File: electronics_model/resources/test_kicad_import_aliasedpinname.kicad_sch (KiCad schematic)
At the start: 3 parts

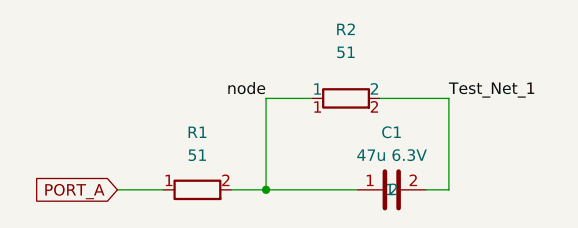
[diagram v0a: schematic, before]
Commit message: unify naming
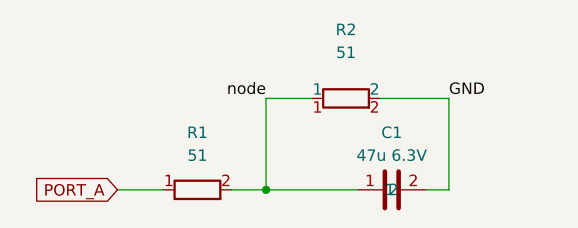
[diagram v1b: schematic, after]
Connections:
- net Test_Net_1 renamed GND
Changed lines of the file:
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@@
     (effects (font (size 1.27 1.27)) (justify right bottom))
   )
-  (label "Test_Net_1" (at 111.76 86.36 0)
+  (label "GND" (at 111.76 86.36 0)
     (effects (font (size 1.27 1.27)) (justify left bottom))
   )
